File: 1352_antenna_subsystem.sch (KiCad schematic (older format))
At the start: 24 parts

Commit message: Recovered the .lib for flash symbol. Relinked in schematic
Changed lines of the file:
@@
 $EndComp
 $Comp
-L power:GND #PWR0201
+L BeagleBone-Black-Cape-rescue:GND-power #PWR0201
 U 1 1 61529DEB
 P 4150 1150
@@
 	3700 1150 3700 1450
 $Comp
-L power:GND #PWR0203
+L BeagleBone-Black-Cape-rescue:GND-power #PWR0203
 U 1 1 6152D8A3
 P 5100 2100
@@
 	4800 2300 5800 2300
 $Comp
-L power:GND #PWR0205
+L BeagleBone-Black-Cape-rescue:GND-power #PWR0205
 U 1 1 615EEDB8
 P 7000 4250
@@
 $EndComp
 $Comp
-L power:GND #PWR0204
+L BeagleBone-Black-Cape-rescue:GND-power #PWR0204
 U 1 1 615F1CB4
 P 6450 5700
@@
 $EndComp
 $Comp
-L power:GND #PWR0206
+L BeagleBone-Black-Cape-rescue:GND-power #PWR0206
 U 1 1 615F4055
 P 7200 5550
@@
 $EndComp
 $Comp
-L power:GND #PWR0207
+L BeagleBone-Black-Cape-rescue:GND-power #PWR0207
 U 1 1 615F600A
 P 7750 5550
@@
 $EndComp
 $Comp
-L power:GND #PWR0208
+L BeagleBone-Black-Cape-rescue:GND-power #PWR0208
 U 1 1 615F8577
 P 8250 5550

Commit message: prepped for PSU subsystem placements
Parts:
- renumbered C3 to C203, C203 to C204, C204 to C205, C205 to C206, C206 to C207, C207 to C208, C208 to C209, C209 to C210, C210 to C211, C211 to C212, C212 to C213
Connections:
- net at C203.2, TF201.1 (ANT_2.4GHz): no longer TF202.8 (SKY_RF3)
- net at C203.1: now also TF202.8 (SKY_RF3)
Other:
- moved on the sheet: C203
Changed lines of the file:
@@
 	6450 5300 6450 5400
 $Comp
-L BeagleBone-Black-Cape-rescue:C-Device C203
+L BeagleBone-Black-Cape-rescue:C-Device C204
 U 1 1 605E8A57
 P 6450 5550
-F 0 "C203" H 6565 5596 50  0000 L CNN
+F 0 "C204" H 6565 5596 50  0000 L CNN
 F 1 "1.2pF" H 6565 5505 50  0000 L CNN
 F 2 "Capacitor_SMD:C_0805_2012Metric_Pad1.18x1.45mm_HandSolder" H 6488 5400 50  0001 C CNN
@@
 	7000 5300 7050 5300
 $Comp
-L BeagleBone-Black-Cape-rescue:C-Device C204
+L BeagleBone-Black-Cape-rescue:C-Device C205
 U 1 1 60611067
 P 6800 4650
-F 0 "C204" V 7050 4600 50  0000 L CNN
+F 0 "C205" V 7050 4600 50  0000 L CNN
 F 1 "1.2pF" V 6950 4550 50  0000 L CNN
 F 2 "Capacitor_SMD:C_0805_2012Metric_Pad1.18x1.45mm_HandSolder" H 6838 4500 50  0001 C CNN
@@
 	7050 5100 7050 5300
 $Comp
-L BeagleBone-Black-Cape-rescue:C-Device C205
+L BeagleBone-Black-Cape-rescue:C-Device C206
 U 1 1 60620B7F
 P 7000 4000
-F 0 "C205" H 7115 4046 50  0000 L CNN
+F 0 "C206" H 7115 4046 50  0000 L CNN
 F 1 "12pF" H 7115 3955 50  0000 L CNN
 F 2 "Capacitor_SMD:C_0805_2012Metric_Pad1.18x1.45mm_HandSolder" H 7038 3850 50  0001 C CNN
@@
 	7000 4150 7400 4150
 $Comp
-L BeagleBone-Black-Cape-rescue:C-Device C207
+L BeagleBone-Black-Cape-rescue:C-Device C208
 U 1 1 6062771A
 P 7400 4000
-F 0 "C207" H 7515 4046 50  0000 L CNN
+F 0 "C208" H 7515 4046 50  0000 L CNN
 F 1 "10nF" H 7515 3955 50  0000 L CNN
 F 2 "Capacitor_SMD:C_0805_2012Metric_Pad1.18x1.45mm_HandSolder" H 7438 3850 50  0001 C CNN
@@
 	7200 5100 7200 5250
 $Comp
-L BeagleBone-Black-Cape-rescue:C-Device C206
+L BeagleBone-Black-Cape-rescue:C-Device C207
 U 1 1 60632FC0
 P 7200 5400
-F 0 "C206" H 7315 5446 50  0000 L CNN
+F 0 "C207" H 7315 5446 50  0000 L CNN
 F 1 "2.7pF" H 7315 5355 50  0000 L CNN
 F 2 "Capacitor_SMD:C_0805_2012Metric_Pad1.18x1.45mm_HandSolder" H 7238 5250 50  0001 C CNN
@@
 	7650 5100 7750 5100
 $Comp
-L BeagleBone-Black-Cape-rescue:C-Device C208
+L BeagleBone-Black-Cape-rescue:C-Device C209
 U 1 1 60645553
 P 7750 5400
-F 0 "C208" H 7865 5446 50  0000 L CNN
+F 0 "C209" H 7865 5446 50  0000 L CNN
 F 1 "1.8pF" H 7865 5355 50  0000 L CNN
 F 2 "Capacitor_SMD:C_0805_2012Metric_Pad1.18x1.45mm_HandSolder" H 7788 5250 50  0001 C CNN
@@
 $EndComp
 $Comp
-L BeagleBone-Black-Cape-rescue:C-Device C209
+L BeagleBone-Black-Cape-rescue:C-Device C210
 U 1 1 60652D1E
 P 8250 5400
-F 0 "C209" H 8365 5446 50  0000 L CNN
+F 0 "C210" H 8365 5446 50  0000 L CNN
 F 1 "1.5pF" H 8365 5355 50  0000 L CNN
 F 2 "Capacitor_SMD:C_0805_2012Metric_Pad1.18x1.45mm_HandSolder" H 8288 5250 50  0001 C CNN
@@
 	8350 4650 8650 4650
 $Comp
-L BeagleBone-Black-Cape-rescue:C-Device C210
+L BeagleBone-Black-Cape-rescue:C-Device C211
 U 1 1 6066C58A
 P 8800 4650
-F 0 "C210" V 9050 4600 50  0000 L CNN
+F 0 "C211" V 9050 4600 50  0000 L CNN
 F 1 "DNF" V 8950 4600 50  0000 L CNN
 F 2 "Capacitor_SMD:C_0805_2012Metric_Pad1.18x1.45mm_HandSolder" H 8838 4500 50  0001 C CNN
@@
 	10200 1650 10200 3300
 $Comp
-L BeagleBone-Black-Cape-rescue:C-Device C211
+L BeagleBone-Black-Cape-rescue:C-Device C212
 U 1 1 6150D584
 P 8850 3300
-F 0 "C211" V 9100 3250 50  0000 L CNN
+F 0 "C212" V 9100 3250 50  0000 L CNN
 F 1 "DNF" V 9000 3250 50  0000 L CNN
 F 2 "Capacitor_SMD:C_0805_2012Metric_Pad1.18x1.45mm_HandSolder" H 8888 3150 50  0001 C CNN
@@
 	8700 3300 8700 3000
 $Comp
-L BeagleBone-Black-Cape-rescue:C-Device C212
+L BeagleBone-Black-Cape-rescue:C-Device C213
 U 1 1 61536BA3
 P 8900 5050
-F 0 "C212" V 9150 5000 50  0000 L CNN
+F 0 "C213" V 9150 5000 50  0000 L CNN
 F 1 "47pF" V 9050 5000 50  0000 L CNN
 F 2 "Capacitor_SMD:C_0805_2012Metric_Pad1.18x1.45mm_HandSolder" H 8938 4900 50  0001 C CNN
@@
 Connection ~ 8350 5100
 $Comp
-L BeagleBone-Black-Cape-rescue:C-Device C3
+L BeagleBone-Black-Cape-rescue:C-Device C203
 U 1 1 614F2671
-P 6000 1550
-F 0 "C3" V 5748 1550 50  0000 C CNN
-F 1 "47pF" V 5839 1550 50  0000 C CNN
-F 2 "Capacitor_SMD:C_0805_2012Metric_Pad1.18x1.45mm_HandSolder" H 6038 1400 50  0001 C CNN
-F 3 "~" H 6000 1550 50  0001 C CNN
-	1    6000 1550
+P 6150 1550
+F 0 "C203" V 5898 1550 50  0000 C CNN
+F 1 "47pF" V 5989 1550 50  0000 C CNN
+F 2 "Capacitor_SMD:C_0805_2012Metric_Pad1.18x1.45mm_HandSolder" H 6188 1400 50  0001 C CNN
+F 3 "~" H 6150 1550 50  0001 C CNN
+	1    6150 1550
 	0    1    1    0
 $EndComp
 Wire Wire Line
-	5850 1550 8250 1550
+	5850 1550 6000 1550
+Wire Wire Line
+	6300 1550 8250 1550
 $EndSCHEMATC

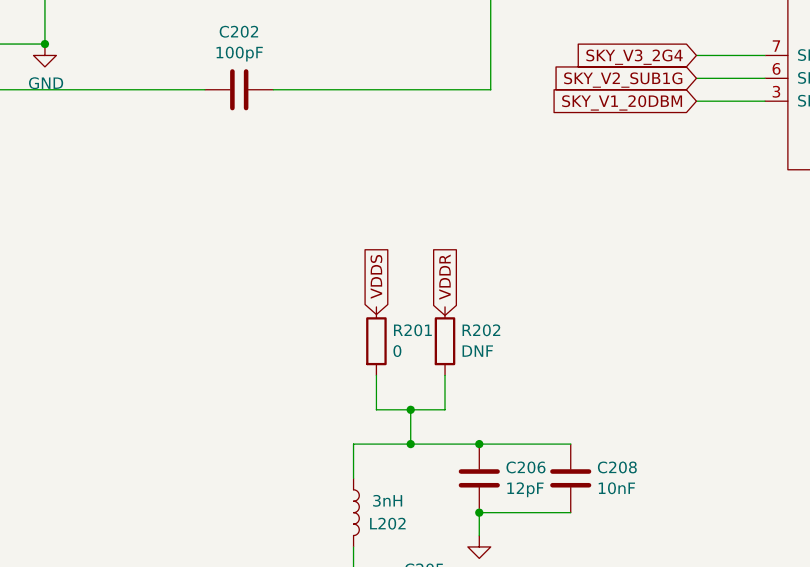
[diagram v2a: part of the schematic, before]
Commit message: Fixed Schematic connection issue and routed some missing traces.
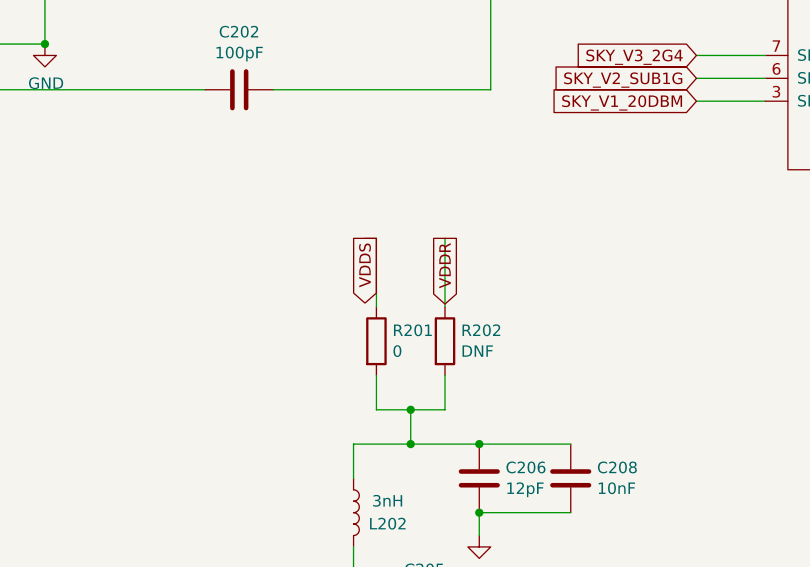
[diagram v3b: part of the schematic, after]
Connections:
- net VDDR: now also R202.1
- net VDDS: now also R201.1
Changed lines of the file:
@@
 	1    0    0    -1
 $EndComp
-Text GLabel 6550 3000 3    50   Output ~ 0
+Text GLabel 6500 2950 3    50   Output ~ 0
 VDDS
-Text GLabel 6850 3000 3    50   Output ~ 0
+Text GLabel 6850 2950 3    50   Output ~ 0
 VDDR
 Connection ~ 7000 3850
@@
 Wire Wire Line
 	6300 1550 8250 1550
+Wire Wire Line
+	6850 2950 6850 3250
+Wire Wire Line
+	6550 3250 6550 2950
+Wire Wire Line
+	6550 2950 6500 2950
 $EndSCHEMATC

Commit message: Last minute fixes before staging for public
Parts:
- L205: footprint Inductor_SMD:L_0805_2012Metric_Pad1.15x1.40mm_HandSolder -> Inductor_SMD:L_0603_1608Metric_Pad1.05x0.95mm_HandSolder
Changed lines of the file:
@@
 F 0 "L205" V 8090 5100 50  0000 C CNN
 F 1 "1nH" V 7999 5100 50  0000 C CNN
-F 2 "Inductor_SMD:L_0805_2012Metric_Pad1.15x1.40mm_HandSolder" H 7900 5100 50  0001 C CNN
+F 2 "Inductor_SMD:L_0603_1608Metric_Pad1.05x0.95mm_HandSolder" H 7900 5100 50  0001 C CNN
 F 3 "~" H 7900 5100 50  0001 C CNN
 	1    7900 5100

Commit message: lib update so it only includes user-made library
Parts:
- AE201, AE202: symbol BeagleBone-Black-Cape-rescue:Antenna-Device -> UserMade-BB-Zigbee-Gateway-CAPE:Antenna-Device
- C201, C202, C203, C204, C205, C206, C207, C208, C209, C210, C211, C212, C213: symbol BeagleBone-Black-Cape-rescue:C-Device -> UserMade-BB-Zigbee-Gateway-CAPE:C-Device
- L201, L202, L203, L204, L205: symbol BeagleBone-Black-Cape-rescue:L-Device -> UserMade-BB-Zigbee-Gateway-CAPE:L-Device
- R201, R202: symbol BeagleBone-Black-Cape-rescue:R-Device -> UserMade-BB-Zigbee-Gateway-CAPE:R-Device
- TF201: symbol cc1352:IPC_1352P -> UserMade-BB-Zigbee-Gateway-CAPE:IPC_1352P
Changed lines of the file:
@@
 $EndDescr
 $Comp
-L BeagleBone-Black-Cape-rescue:GND-power #PWR0202
+L UserMade-BB-Zigbee-Gateway-CAPE:GND-power #PWR0202
 U 1 1 603D2468
 P 4400 3350
@@
 	4100 3350 4400 3350
 $Comp
-L BeagleBone-Black-Cape-rescue:C-Device C201
+L UserMade-BB-Zigbee-Gateway-CAPE:C-Device C201
 U 1 1 603D700A
 P 3950 3350
@@
 TX_20dB_N
 $Comp
-L BeagleBone-Black-Cape-rescue:L-Device L203
+L UserMade-BB-Zigbee-Gateway-CAPE:L-Device L203
 U 1 1 605CA70F
 P 6850 5300
@@
 $EndComp
 $Comp
-L BeagleBone-Black-Cape-rescue:L-Device L201
+L UserMade-BB-Zigbee-Gateway-CAPE:L-Device L201
 U 1 1 605D71FC
 P 6150 4950
@@
 	6450 5300 6450 5400
 $Comp
-L BeagleBone-Black-Cape-rescue:C-Device C204
+L UserMade-BB-Zigbee-Gateway-CAPE:C-Device C204
 U 1 1 605E8A57
 P 6450 5550
@@
 $EndComp
 $Comp
-L BeagleBone-Black-Cape-rescue:L-Device L202
+L UserMade-BB-Zigbee-Gateway-CAPE:L-Device L202
 U 1 1 605F1A20
 P 6450 4150
@@
 	7000 5300 7050 5300
 $Comp
-L BeagleBone-Black-Cape-rescue:C-Device C205
+L UserMade-BB-Zigbee-Gateway-CAPE:C-Device C205
 U 1 1 60611067
 P 6800 4650
@@
 	7050 5100 7050 5300
 $Comp
-L BeagleBone-Black-Cape-rescue:C-Device C206
+L UserMade-BB-Zigbee-Gateway-CAPE:C-Device C206
 U 1 1 60620B7F
 P 7000 4000
@@
 	7000 4150 7400 4150
 $Comp
-L BeagleBone-Black-Cape-rescue:C-Device C208
+L UserMade-BB-Zigbee-Gateway-CAPE:C-Device C208
 U 1 1 6062771A
 P 7400 4000
@@
 	7200 5100 7200 5250
 $Comp
-L BeagleBone-Black-Cape-rescue:C-Device C207
+L UserMade-BB-Zigbee-Gateway-CAPE:C-Device C207
 U 1 1 60632FC0
 P 7200 5400
@@
 Connection ~ 7200 5100
 $Comp
-L BeagleBone-Black-Cape-rescue:L-Device L204
+L UserMade-BB-Zigbee-Gateway-CAPE:L-Device L204
 U 1 1 606403DF
 P 7500 5100
@@
 	7650 5100 7750 5100
 $Comp
-L BeagleBone-Black-Cape-rescue:C-Device C209
+L UserMade-BB-Zigbee-Gateway-CAPE:C-Device C209
 U 1 1 60645553
 P 7750 5400
@@
 	7750 5100 7750 5250
 $Comp
-L BeagleBone-Black-Cape-rescue:L-Device L205
+L UserMade-BB-Zigbee-Gateway-CAPE:L-Device L205
 U 1 1 6064D542
 P 7900 5100
@@
 $EndComp
 $Comp
-L BeagleBone-Black-Cape-rescue:C-Device C210
+L UserMade-BB-Zigbee-Gateway-CAPE:C-Device C210
 U 1 1 60652D1E
 P 8250 5400
@@
 	8350 4650 8650 4650
 $Comp
-L BeagleBone-Black-Cape-rescue:C-Device C211
+L UserMade-BB-Zigbee-Gateway-CAPE:C-Device C211
 U 1 1 6066C58A
 P 8800 4650
@@
 $EndComp
 $Comp
-L BeagleBone-Black-Cape-rescue:Antenna-Device AE202
+L UserMade-BB-Zigbee-Gateway-CAPE:Antenna-Device AE202
 U 1 1 6066FAEC
 P 8950 4150
@@
 	8950 4650 8950 4350
 $Comp
-L BeagleBone-Black-Cape-rescue:R-Device R201
+L UserMade-BB-Zigbee-Gateway-CAPE:R-Device R201
 U 1 1 6067AEFA
 P 6550 3400
@@
 $EndComp
 $Comp
-L BeagleBone-Black-Cape-rescue:R-Device R202
+L UserMade-BB-Zigbee-Gateway-CAPE:R-Device R202
 U 1 1 6067CE21
 P 6850 3400
@@
 	2800 3350 3700 3350
 $Comp
-L cc1352:IPC_1352P TF201
+L UserMade-BB-Zigbee-Gateway-CAPE:IPC_1352P TF201
 U 1 1 61528E3E
 P 3700 2050
@@
 $EndComp
 $Comp
-L BeagleBone-Black-Cape-rescue:GND-power #PWR0201
+L UserMade-BB-Zigbee-Gateway-CAPE:GND-power #PWR0201
 U 1 1 61529DEB
 P 4150 1150
@@
 	3700 1150 3700 1450
 $Comp
-L BeagleBone-Black-Cape-rescue:GND-power #PWR0203
+L UserMade-BB-Zigbee-Gateway-CAPE:GND-power #PWR0203
 U 1 1 6152D8A3
 P 5100 2100
@@
 	3700 3350 3800 3350
 $Comp
-L BeagleBone-Black-Cape-rescue:C-Device C202
+L UserMade-BB-Zigbee-Gateway-CAPE:C-Device C202
 U 1 1 615A901D
 P 5950 2300
@@
 	4800 2300 5800 2300
 $Comp
-L BeagleBone-Black-Cape-rescue:GND-power #PWR0205
+L UserMade-BB-Zigbee-Gateway-CAPE:GND-power #PWR0205
 U 1 1 615EEDB8
 P 7000 4250
@@
 $EndComp
 $Comp
-L BeagleBone-Black-Cape-rescue:GND-power #PWR0204
+L UserMade-BB-Zigbee-Gateway-CAPE:GND-power #PWR0204
 U 1 1 615F1CB4
 P 6450 5700
@@
 $EndComp
 $Comp
-L BeagleBone-Black-Cape-rescue:GND-power #PWR0206
+L UserMade-BB-Zigbee-Gateway-CAPE:GND-power #PWR0206
 U 1 1 615F4055
 P 7200 5550
@@
 $EndComp
 $Comp
-L BeagleBone-Black-Cape-rescue:GND-power #PWR0207
+L UserMade-BB-Zigbee-Gateway-CAPE:GND-power #PWR0207
 U 1 1 615F600A
 P 7750 5550
@@
 $EndComp
 $Comp
-L BeagleBone-Black-Cape-rescue:GND-power #PWR0208
+L UserMade-BB-Zigbee-Gateway-CAPE:GND-power #PWR0208
 U 1 1 615F8577
 P 8250 5550
@@
 	9950 1450 9950 1500
 $Comp
-L BeagleBone-Black-Cape-rescue:GND-power #PWR0209
+L UserMade-BB-Zigbee-Gateway-CAPE:GND-power #PWR0209
 U 1 1 61500151
 P 9950 1500
@@
 	10200 1650 10200 3300
 $Comp
-L BeagleBone-Black-Cape-rescue:C-Device C212
+L UserMade-BB-Zigbee-Gateway-CAPE:C-Device C212
 U 1 1 6150D584
 P 8850 3300
@@
 $EndComp
 $Comp
-L BeagleBone-Black-Cape-rescue:Antenna-Device AE201
+L UserMade-BB-Zigbee-Gateway-CAPE:Antenna-Device AE201
 U 1 1 615152E3
 P 8700 2800
@@
 	8700 3300 8700 3000
 $Comp
-L BeagleBone-Black-Cape-rescue:C-Device C213
+L UserMade-BB-Zigbee-Gateway-CAPE:C-Device C213
 U 1 1 61536BA3
 P 8900 5050
@@
 Connection ~ 8350 5100
 $Comp
-L BeagleBone-Black-Cape-rescue:C-Device C203
+L UserMade-BB-Zigbee-Gateway-CAPE:C-Device C203
 U 1 1 614F2671
 P 6150 1550

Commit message: final edits before it'll be untouched
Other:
- moved on the sheet: AE201, AE202, C201, C202, C203, C204, C205, C206, C207, C208, C209, C210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
